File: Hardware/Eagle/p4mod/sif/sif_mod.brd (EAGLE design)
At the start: 19.6 x 10.8 mm, 29 parts

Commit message: Lowered values of the segment resistors for the Sif board.
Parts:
- R2, R3, R4, R5, R6, R7, R8: value 82 -> 75
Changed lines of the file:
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@@
 <element name="C2" library="resistor_mod" package="C0402K" value="0.1 uF" x="5.489228125" y="7.27175" rot="MR270"/>
 <element name="CEFC" library="resistor_mod" package="C0402K" value="10 uF" x="15.7456375" y="2.018803125" rot="MR180"/>
-<element name="R2" library="resistor_mod" package="R0402" value="82" x="8.3567125" y="1.48803125"/>
-<element name="R3" library="resistor_mod" package="R0402" value="82" x="17.8972875" y="9.51516875"/>
-<element name="R4" library="resistor_mod" package="R0402" value="82" x="1.736546875" y="2.76519375" rot="R270"/>
-<element name="R5" library="resistor_mod" package="R0402" value="82" x="2.762284375" y="9.32258125" rot="R180"/>
-<element name="R6" library="resistor_mod" package="R0402" value="82" x="20.19658125" y="2.78789375" rot="R270"/>
-<element name="R7" library="resistor_mod" package="R0402" value="82" x="5.1324125" y="8.652253125" rot="R180"/>
-<element name="R8" library="resistor_mod" package="R0402" value="82" x="5.881634375" y="10.324834375" rot="R180"/>
+<element name="R2" library="resistor_mod" package="R0402" value="75" x="8.3567125" y="1.48803125"/>
+<element name="R3" library="resistor_mod" package="R0402" value="75" x="17.8972875" y="9.51516875"/>
+<element name="R4" library="resistor_mod" package="R0402" value="75" x="1.736546875" y="2.76519375" rot="R270"/>
+<element name="R5" library="resistor_mod" package="R0402" value="75" x="2.762284375" y="9.32258125" rot="R180"/>
+<element name="R6" library="resistor_mod" package="R0402" value="75" x="20.19658125" y="2.78789375" rot="R270"/>
+<element name="R7" library="resistor_mod" package="R0402" value="75" x="5.1324125" y="8.652253125" rot="R180"/>
+<element name="R8" library="resistor_mod" package="R0402" value="75" x="5.881634375" y="10.324834375" rot="R180"/>
 <element name="C4" library="resistor_mod" package="C0402K" value="12 pF" x="4.124525" y="5.199515625" rot="MR90"/>
 <element name="R16" library="resistor_mod" package="R0402" value="4.7k" x="16.721203125" y="3.62945" rot="MR180"/>

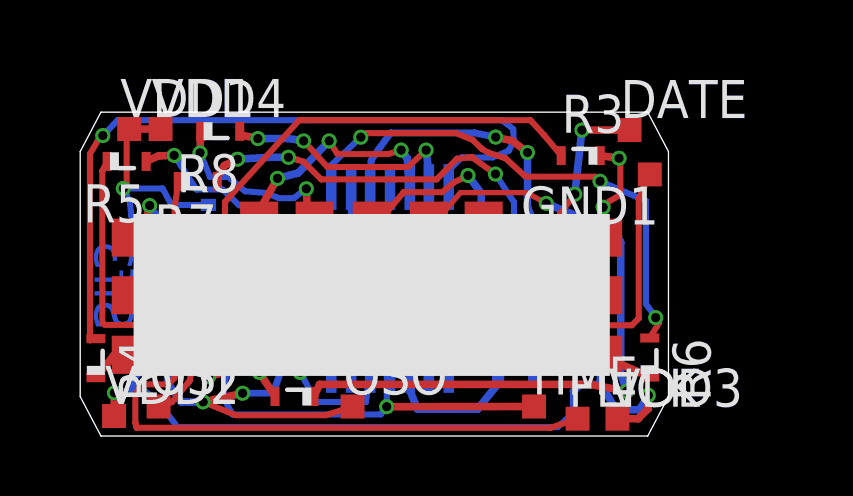
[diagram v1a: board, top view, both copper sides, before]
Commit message: Upgraded Sif module to use nmos transistors for the common cathodes.
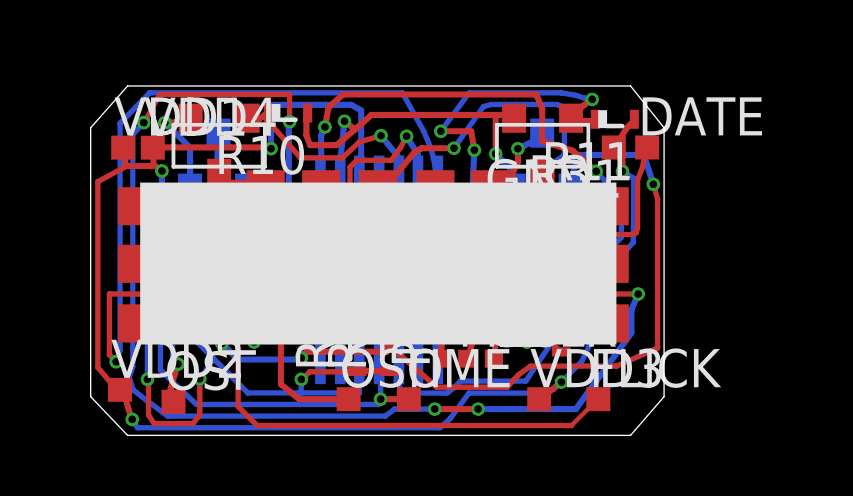
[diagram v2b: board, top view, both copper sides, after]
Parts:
- added Q1, Q2, Q3, Q4: IRLML0030, irlml0030:SOT-23
- added R10, R11, R12, R9: 47k, resistor_mod:R0402
- R2, R3, R4, R5, R6, R7, R8: value 75 -> 82
- moved R5 15.0 mm to (17.3, 5.63), turned to 90 degrees
- moved PGC 9.85 mm to (13.3, 2.75), flipped to the top, turned to 90 degrees
- moved R2 6.69 mm to (13.0, 6.30)
- moved R8 5.15 mm to (9.55, 6.71)
- moved TIME 4.18 mm to (12.2, 1.40)
- moved R4 3.59 mm to (5.04, 4.17)
- moved R17 3.25 mm to (4.07, 6.00), turned to 90 degrees
- moved R16 3.22 mm to (18.4, 6.40), turned to 270 degrees
- moved PGD 3.15 mm to (14.1, 2.75), flipped to the top
- moved R6 3.06 mm to (17.3, 3.62), turned to 90 degrees
- moved MCLR 2.79 mm to (15.0, 2.75), flipped to the top
- moved VDD3 2.69 mm to (16.5, 1.40)
- moved CEFC 2.56 mm to (17.0, 4.24), turned to 90 degrees
- moved R7 2.49 mm to (4.93, 6.17), turned to 270 degrees
- moved R3 2.31 mm to (16.8, 7.50)
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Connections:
- new net N$11: Q2.P3, U$2.P$9_KATHODE_10_MIN
- new net N$12: Q3.P3, U$2.P$10_KATHODE_1_HOUR
- new net N$13: Q4.P3, U$2.P$11_KATHODE_10_HOUR
- new net N$14: Q1.P3, U$2.P$8_KATHODE_1_MIN
- net GND: now also Q1.P2, Q2.P2, Q3.P2, Q4.P2, R10.1, R11.1, R12.1, R9.1
- net PGC/LED_M7: now also Q4.P1, R9.2; no longer U$2.P$11_KATHODE_10_HOUR
- net RB1/LED_M6: now also Q3.P1, R10.2; no longer U$2.P$10_KATHODE_1_HOUR
- net RB4/LED_H4: now also Q2.P1, R11.2; no longer U$2.P$9_KATHODE_10_MIN
- net RC3/LED_M4: now also Q1.P1, R12.2; no longer U$2.P$8_KATHODE_1_MIN
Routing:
- net RC6/LED_M1: track 6.06 -> 41.1 mm, vias 1 -> 5
- net N$7: track 24.6 -> 1.67 mm
- net N$10: track 23.2 -> 1.96 mm, vias 2 -> 0
- net RC3/LED_M4: track 9.92 -> 30.3 mm, vias 1 -> 4
- net GND: track 42.1 -> 62.5 mm, vias 3 -> 7
- net N$11: track 0.00 -> 12.1 mm, vias 0 -> 2
- net VDD: track 52.1 -> 43.3 mm, vias 5 -> 4
- net RB4/LED_H4: track 5.63 -> 11.8 mm, vias 1 -> 3
- net N$1: track 23.4 -> 17.7 mm
- net N$13: track 0.00 -> 5.49 mm, vias 0 -> 1
- net N$2: track 6.73 -> 1.50 mm, vias 2 -> 0
- net RC7/LED_M5: track 17.2 -> 21.5 mm
- net T1OSO: track 13.8 -> 9.97 mm
- net PGD/RB7: track 1.20 -> 4.84 mm, vias 0 -> 1
- net N$14: track 0.00 -> 3.37 mm, vias 0 -> 1
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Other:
- board size 19.6 x 10.8 mm -> 19.1 x 11.6 mm
- board text removed: "Sif3"

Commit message: Updated footprint of 10 uF ceramic cap to 0602.
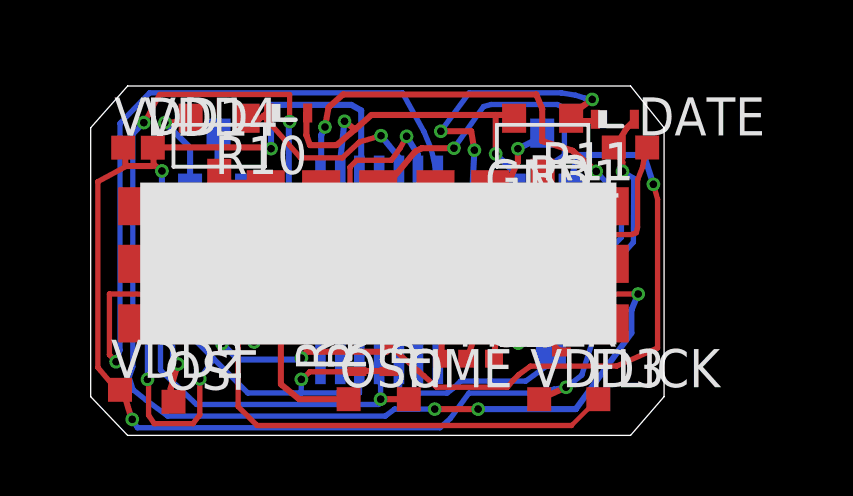
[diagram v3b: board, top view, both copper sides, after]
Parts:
- CEFC: device resistor_mod:C0402K -> rcl:C0603
- moved CEFC 0.44 mm to (16.9, 3.81)
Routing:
- net MCLR: track 6.69 -> 7.29 mm
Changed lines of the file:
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@@
 <element name="R1" library="resistor_mod" package="R0402" value="10K" x="18.35831875" y="4.3688" rot="MR90"/>
 <element name="C2" library="resistor_mod" package="C0402K" value="0.1 uF" x="4.553640625" y="7.308175" rot="MR180"/>
-<element name="CEFC" library="resistor_mod" package="C0402K" value="10 uF" x="17.0235375" y="4.238140625" rot="MR90"/>
+<element name="CEFC" library="rcl" package="C0603" value="10 uF" x="16.90450625" y="3.814696875" rot="MR90"/>
 <element name="R2" library="resistor_mod" package="R0402" value="82" x="13.008109375" y="6.29623125"/>
 <element name="R3" library="resistor_mod" package="R0402" value="82" x="16.778290625" y="7.4951875"/>
@@
 <wire x1="18.2118" y1="5.7404" x2="17.9486" y2="5.640896875" width="0.2032" layer="16"/>
 <wire x1="18.6182" y1="5.7404" x2="18.2118" y2="5.7404" width="0.2032" layer="16"/>
-<wire x1="17.63333125" y1="5.351959375" x2="17.0235375" y2="4.838140625" width="0.2032" layer="16"/>
+<wire x1="17.63333125" y1="5.351959375" x2="16.90450625" y2="4.664696875" width="0.2032" layer="16"/>
 <wire x1="18.6182" y1="5.7404" x2="18.35831875" y2="5.752271875" width="0.1524" layer="16"/>
 <wire x1="16.044090625" y1="7.874240625" x2="15.6718" y2="8.6614" width="0.1778" layer="16"/>
@@
 <wire x1="17.149721875" y1="4.9280625" x2="16.953615625" y2="4.927359375" width="0.1778" layer="16"/>
 <wire x1="15.6718" y1="8.6614" x2="15.662915625" y2="8.429753125" width="0.1524" layer="16"/>
-<wire x1="17.149721875" y1="4.9280625" x2="17.0235375" y2="4.838140625" width="0.1778" layer="16"/>
+<wire x1="17.149721875" y1="4.9280625" x2="16.90450625" y2="4.664696875" width="0.1778" layer="16"/>
 <wire x1="19.2863125" y1="9.29944375" x2="19.14893125" y2="9.619784375" width="0.2032" layer="1"/>
 <wire x1="19.289003125" y1="8.99136875" x2="19.2863125" y2="9.29944375" width="0.2032" layer="1"/>
@@
 <wire x1="14.2494" y1="5.0292" x2="14.22529375" y2="5.0471375" width="0.1524" layer="16"/>
 <wire x1="18.42038125" y1="4.999584375" x2="18.43093125" y2="5.010571875" width="0.2032" layer="16"/>
-<wire x1="18.274" y1="4.78273125" x2="18.42038125" y2="4.999584375" width="0.2032" layer="16"/>
-<wire x1="18.11581875" y1="4.5974" x2="18.274" y2="4.78273125" width="0.2032" layer="16"/>
-<wire x1="17.818125" y1="4.244521875" x2="18.11581875" y2="4.5974" width="0.2032" layer="16"/>
+<wire x1="18.08413125" y1="4.991215625" x2="18.42038125" y2="4.999584375" width="0.1778" layer="16"/>
+<wire x1="17.907425" y1="4.68543125" x2="18.08413125" y2="4.991215625" width="0.1778" layer="16"/>
+<wire x1="17.70698125" y1="3.81829375" x2="17.907425" y2="4.68543125" width="0.1778" layer="16"/>
 <wire x1="18.43093125" y1="5.010571875" x2="18.35831875" y2="5.0188" width="0.1778" layer="16"/>
 <via x="15.494784375" y="4.222415625" extent="1-16" drill="0.254"/>
-<wire x1="17.818125" y1="4.244521875" x2="16.195475" y2="4.24475625" width="0.2032" layer="16"/>
-<wire x1="16.195475" y1="4.24475625" x2="15.494784375" y2="4.222415625" width="0.2032" layer="16"/>
+<wire x1="17.70698125" y1="3.81829375" x2="16.3019875" y2="3.818290625" width="0.1778" layer="16"/>
+<wire x1="16.3019875" y1="3.818290625" x2="15.494784375" y2="4.222415625" width="0.1778" layer="16"/>
 </signal>
 <signal name="VDD">
@@
 <contactref element="VDD3" pad="TP"/>
 <contactref element="VDD4" pad="TP"/>
-<wire x1="17.932009375" y1="2.656590625" x2="18.36290625" y2="3.559665625" width="0.1778" layer="16"/>
-<wire x1="17.256028125" y1="1.966671875" x2="17.932009375" y2="2.656590625" width="0.1778" layer="16"/>
-<wire x1="16.5354" y1="1.397" x2="17.256028125" y2="1.966671875" width="0.2032" layer="1"/>
+<wire x1="17.932009375" y1="2.19503125" x2="18.36290625" y2="3.559665625" width="0.1778" layer="16"/>
+<wire x1="17.409721875" y1="1.7935875" x2="17.932009375" y2="2.19503125" width="0.1778" layer="16"/>
+<wire x1="16.5354" y1="1.397" x2="17.409721875" y2="1.7935875" width="0.2032" layer="1"/>
 <wire x1="18.36290625" y1="3.559665625" x2="18.35831875" y2="3.7188" width="0.1778" layer="16"/>
 <wire x1="16.5354" y1="1.397" x2="16.511784375" y2="1.397" width="0.1524" layer="1"/>
@@
 <wire x1="2.88275" y1="0.8789625" x2="2.947496875" y2="0.7245875" width="0.2032" layer="1"/>
 <wire x1="2.7432" y1="1.3462" x2="2.88275" y2="0.8789625" width="0.2032" layer="1"/>
-<wire x1="16.99943125" y1="1.7299375" x2="17.256028125" y2="1.966671875" width="0.1778" layer="16"/>
+<wire x1="16.99943125" y1="1.7299375" x2="17.409721875" y2="1.7935875" width="0.1778" layer="16"/>
 <wire x1="2.7432" y1="1.3462" x2="2.5390625" y2="1.708484375" width="0.1778" layer="1"/>
-<via x="17.256028125" y="1.966671875" extent="1-16" drill="0.254"/>
+<via x="17.409721875" y="1.7935875" extent="1-16" drill="0.254"/>
 <via x="3.937" y="9.0056125" extent="1-16" drill="0.254"/>
 <via x="7.574740625" y="9.748059375" extent="1-16" drill="0.254"/>
@@
 <wire x1="16.64081875" y1="5.412734375" x2="16.64081875" y2="3.787134375" width="0.1778" layer="1"/>
 <wire x1="16.8473875" y1="5.67599375" x2="16.64081875" y2="5.412734375" width="0.1778" layer="1"/>
-<wire x1="17.94020625" y1="6.364653125" x2="16.8473875" y2="5.67599375" width="0.1778" layer="16"/>
-<wire x1="18.650334375" y1="6.364653125" x2="17.94020625" y2="6.364653125" width="0.1778" layer="16"/>
-<wire x1="19.07163125" y1="6.6029875" x2="18.650334375" y2="6.364653125" width="0.1778" layer="16"/>
+<wire x1="17.935575" y1="6.397084375" x2="16.8473875" y2="5.67599375" width="0.1778" layer="16"/>
+<wire x1="18.645703125" y1="6.397084375" x2="17.935575" y2="6.397084375" width="0.1778" layer="16"/>
+<wire x1="19.07163125" y1="6.6029875" x2="18.645703125" y2="6.397084375" width="0.1778" layer="16"/>
 <wire x1="19.2532" y1="6.79210625" x2="19.07163125" y2="6.6029875" width="0.1778" layer="16"/>
 <wire x1="19.2532" y1="8.0772" x2="19.2532" y2="6.79210625" width="0.1778" layer="16"/>
@@
 <wire x1="17.480440625" y1="6.979334375" x2="18.145603125" y2="7.02315625" width="0.2032" layer="16"/>
 <wire x1="16.836784375" y1="6.91573125" x2="17.480440625" y2="6.979334375" width="0.2032" layer="16"/>
-<wire x1="16.102609375" y1="3.300290625" x2="16.25609375" y2="4.220715625" width="0.1778" layer="1"/>
-<wire x1="14.2494" y1="3.81" x2="16.102609375" y2="3.300290625" width="0.2032" layer="16"/>
+<wire x1="15.820121875" y1="3.263225" x2="16.25609375" y2="4.220715625" width="0.1778" layer="1"/>
+<wire x1="14.2494" y1="3.81" x2="15.820121875" y2="3.263225" width="0.2032" layer="16"/>
 <wire x1="14.2494" y1="3.7592" x2="14.2494" y2="3.81" width="0.1524" layer="16"/>
 <wire x1="18.145603125" y1="7.02315625" x2="18.35831875" y2="7.052271875" width="0.1778" layer="16"/>
@@
 <wire x1="16.91094375" y1="6.8834" x2="19.5834" y2="6.8834" width="0.1778" layer="1"/>
 <via x="16.836784375" y="6.91573125" extent="1-16" drill="0.254"/>
-<via x="16.102609375" y="3.300290625" extent="1-16" drill="0.254"/>
+<via x="15.820121875" y="3.263225" extent="1-16" drill="0.254"/>
 <wire x1="16.25609375" y1="4.220715625" x2="16.25609375" y2="5.60870625" width="0.1778" layer="1"/>
 <wire x1="16.25609375" y1="5.60870625" x2="16.273025" y2="5.8146625" width="0.1778" layer="1"/>
@@
 <contactref element="U$1" pad="3"/>
 <contactref element="CEFC" pad="1"/>
-<wire x1="16.067421875" y1="2.0007625" x2="17.042984375" y2="3.455175" width="0.1778" layer="16"/>
+<wire x1="16.067421875" y1="2.0007625" x2="16.987415625" y2="2.667575" width="0.1778" layer="16"/>
 <wire x1="13.894709375" y1="2.0007625" x2="16.067421875" y2="2.0007625" width="0.1778" layer="16"/>
 <wire x1="13.6795875" y1="1.784521875" x2="13.894709375" y2="2.0007625" width="0.1778" layer="16"/>
@@
 <wire x1="11.8618" y1="1.6002" x2="13.44311875" y2="1.6002" width="0.1778" layer="16"/>
 <wire x1="11.8618" y1="2.6416" x2="11.8618" y2="1.6002" width="0.1778" layer="16"/>
-<wire x1="17.042984375" y1="3.455175" x2="17.0235375" y2="3.638140625" width="0.1778" layer="16"/>
+<wire x1="16.987415625" y1="2.667575" x2="16.90450625" y2="2.964696875" width="0.1778" layer="16"/>
 <wire x1="11.8618" y1="2.6416" x2="11.83769375" y2="2.6595375" width="0.1524" layer="16"/>
 </signal>

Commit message: Moved Frist Flick pads.
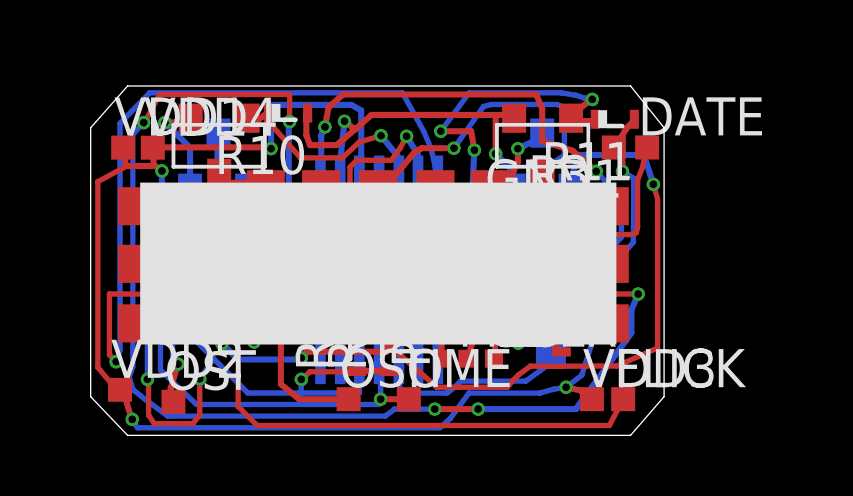
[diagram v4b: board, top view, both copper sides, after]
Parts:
- moved VDD3 1.76 mm to (18.3, 1.40)
- moved FLICK 0.83 mm to (19.3, 1.40)
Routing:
- net N$1: track 17.7 -> 18.7 mm
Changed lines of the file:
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@@
 <attribute name="TP_SIGNAL_NAME" value="" x="10.16" y="1.397" size="1.778" layer="27" display="off"/>
 </element>
-<element name="FLICK" library="testpad" package="TP08SQ" value="TPTP08SQ" x="18.48399375" y="1.397">
-<attribute name="TP_SIGNAL_NAME" value="" x="18.48399375" y="1.397" size="1.778" layer="27" display="off"/>
+<element name="FLICK" library="testpad" package="TP08SQ" value="TPTP08SQ" x="19.3141125" y="1.397">
+<attribute name="TP_SIGNAL_NAME" value="" x="19.3141125" y="1.397" size="1.778" layer="27" display="off"/>
 </element>
 <element name="TIME" library="testpad" package="TP08SQ" value="TPTP08SQ" x="12.1666" y="1.397">
@@
 <attribute name="TP_SIGNAL_NAME" value="" x="2.5390625" y="1.708484375" size="1.778" layer="27" display="off"/>
 </element>
-<element name="VDD3" library="testpad" package="TP08SQ" value="TPTP08SQ" x="16.511784375" y="1.397">
-<attribute name="TP_SIGNAL_NAME" value="" x="16.511784375" y="1.397" size="1.778" layer="27" display="off"/>
+<element name="VDD3" library="testpad" package="TP08SQ" value="TPTP08SQ" x="18.268871875" y="1.397">
+<attribute name="TP_SIGNAL_NAME" value="" x="18.268871875" y="1.397" size="1.778" layer="27" display="off"/>
 </element>
 <element name="VDD4" library="testpad" package="TP08SQ" value="TPTP08SQ" x="3.633571875" y="9.779">
@@
 <wire x1="17.932009375" y1="2.19503125" x2="18.36290625" y2="3.559665625" width="0.1778" layer="16"/>
 <wire x1="17.409721875" y1="1.7935875" x2="17.932009375" y2="2.19503125" width="0.1778" layer="16"/>
-<wire x1="16.5354" y1="1.397" x2="17.409721875" y2="1.7935875" width="0.2032" layer="1"/>
+<wire x1="17.8912625" y1="1.68776875" x2="17.409721875" y2="1.7935875" width="0.2032" layer="1"/>
 <wire x1="18.36290625" y1="3.559665625" x2="18.35831875" y2="3.7188" width="0.1778" layer="16"/>
-<wire x1="16.5354" y1="1.397" x2="16.511784375" y2="1.397" width="0.1524" layer="1"/>
+<wire x1="17.8912625" y1="1.68776875" x2="18.268871875" y2="1.397" width="0.2032" layer="1"/>
 <wire x1="3.937" y1="9.0056125" x2="3.937" y2="7.3152" width="0.2032" layer="16"/>
 <wire x1="3.6576" y1="9.2202" x2="3.937" y2="9.0056125" width="0.2032" layer="1"/>
@@
 <wire x1="8.128" y1="5.0292" x2="8.12929375" y2="5.0471375" width="0.1524" layer="16"/>
 <via x="6.477" y="4.2418" extent="1-16" drill="0.254"/>
-<wire x1="17.6022" y1="0.5334" x2="18.4658" y2="1.397" width="0.1524" layer="1"/>
-<wire x1="18.4658" y1="1.397" x2="18.48399375" y2="1.397" width="0.1524" layer="1"/>
+<wire x1="17.6022" y1="0.519978125" x2="18.8531875" y2="0.519978125" width="0.1778" layer="1"/>
+<wire x1="18.8531875" y1="0.519978125" x2="19.3141125" y2="1.397" width="0.1778" layer="1"/>
 <wire x1="6.477" y1="4.2418" x2="6.477" y2="1.154878125" width="0.1778" layer="1"/>
 <wire x1="6.477" y1="1.154878125" x2="7.1119" y2="0.519978125" width="0.1778" layer="1"/>
-<wire x1="7.1119" y1="0.519978125" x2="17.588778125" y2="0.519978125" width="0.1778" layer="1"/>
-<wire x1="17.588778125" y1="0.519978125" x2="17.6022" y2="0.5334" width="0.1778" layer="1"/>
+<wire x1="7.1119" y1="0.519978125" x2="17.6022" y2="0.519978125" width="0.1778" layer="1"/>
 </signal>
 <signal name="N$2">
